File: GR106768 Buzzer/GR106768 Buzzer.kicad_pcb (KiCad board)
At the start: 4 copper layers, 76 x 58 mm, 342 parts, among them IC1 L-BC-SOT23-5, IC2 L-BC-SO08, IC3 L-BC-SO08, IC4 L-BC-SOT23-5, IC5 L-BC-SO08, IC6 L-BC-SO08, IC7 L-BC-SOT23-6, IC8 L-BC-DFN10, IC9 L-BC-SOT23-6, J1 BAR-10-1007, J2 MIRECMS, J3 MIRECMS, SW1 SI-10-NK236, T1 Q-BC-SOT23-BEC, T10 Q-BC-SOT23-GSD, T11 Q-BC-SOT23-GSD, T12 Q-BC-SOT23-GSD, T13 Q-BC-SOT23-GSD, T2 Q-BC-SOT23-BEC, T3 Q-BC-SOT23-BEC, T4 Q-BC-SOT23-BEC, T5 Q-BC-SOT23-GSD, T6 Q-BC-SOT23-GSD, T7 Q-BC-SOT23-GSD, T8 Q-BC-SOT23-GSD, T9 Q-BC-SOT23-GSD

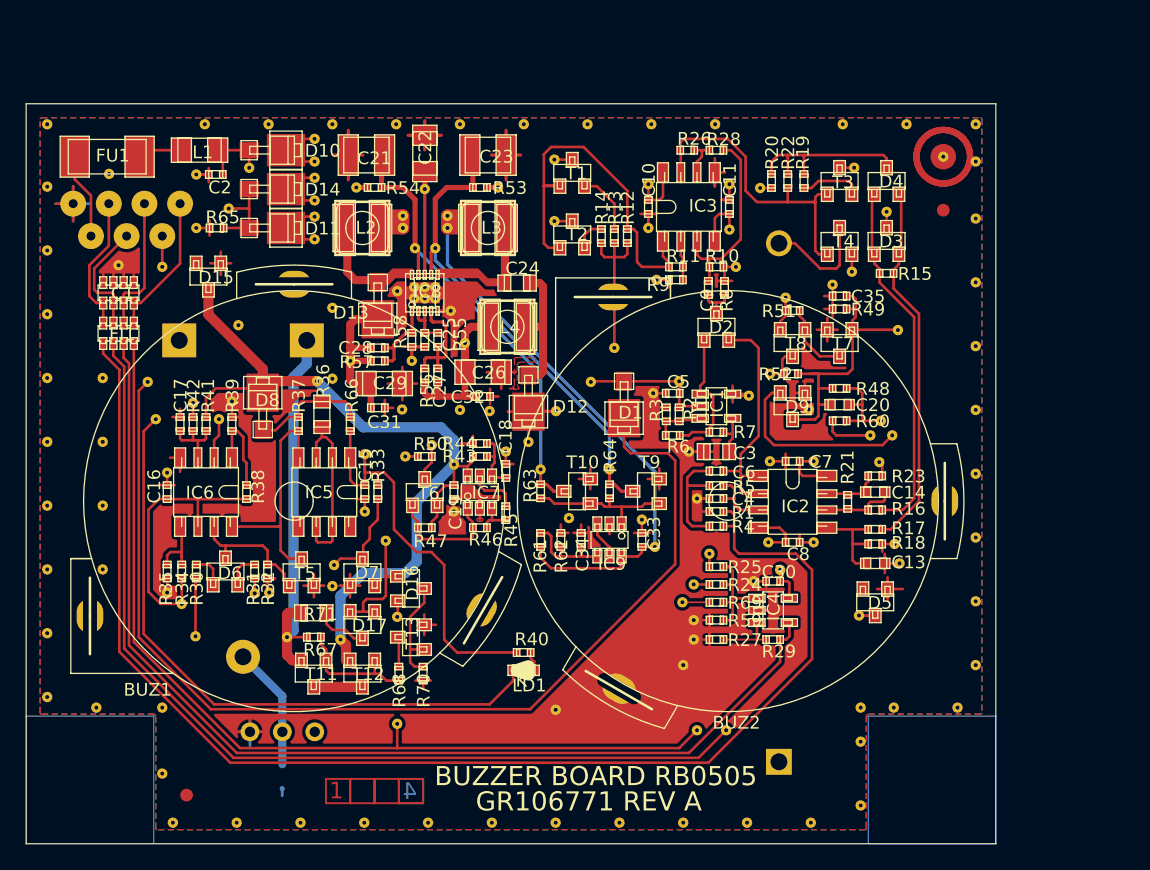
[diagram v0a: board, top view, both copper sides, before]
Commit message: buzzer PCB updates
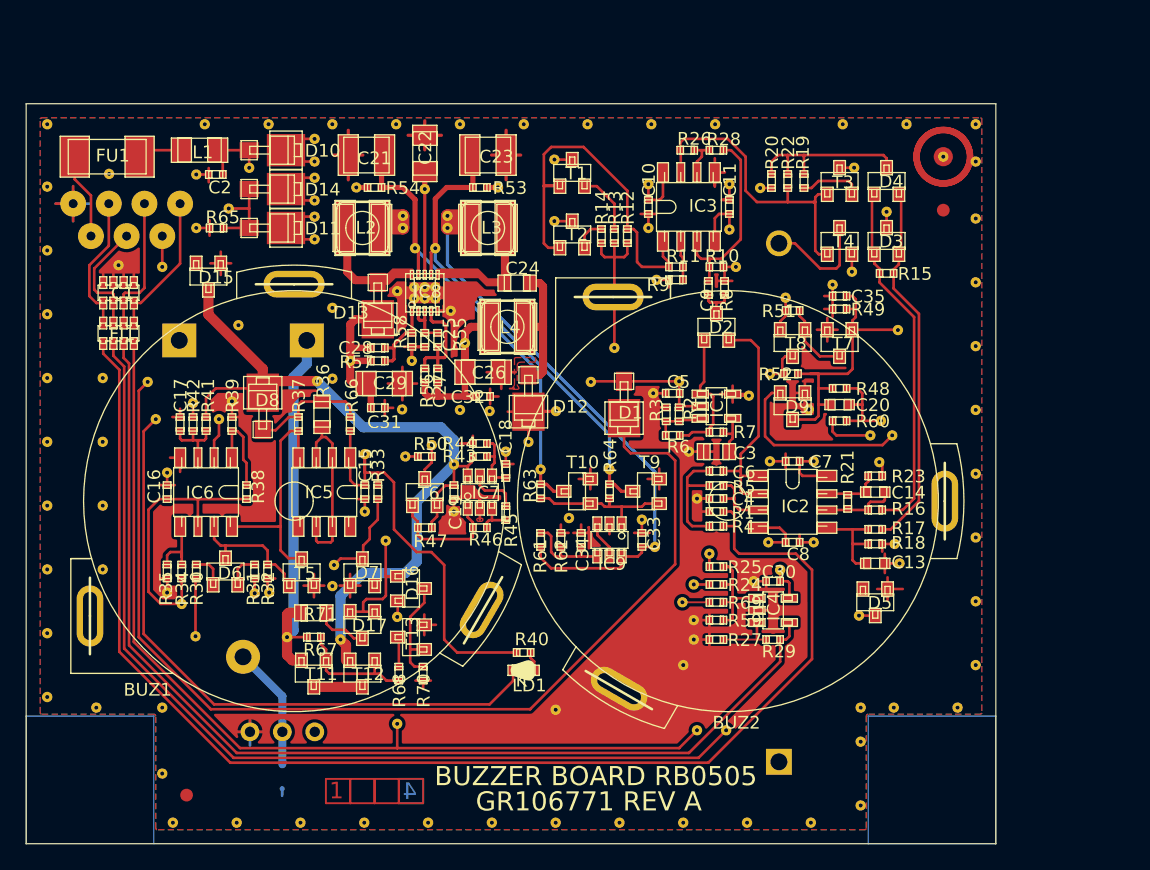
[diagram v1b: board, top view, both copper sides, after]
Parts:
- BUZ1: footprint PKM33EPH-1201C_101110111001 -> AllModules:PKM33EPH-1201C_101110111001
- BUZ2: footprint PKM33EPH-1201C_100110111001 -> AllModules:PKM33EPH-1201C_100110111001
- JP1: footprint TB-CMS-AIROX -> AllModules:TB-CMS-AIROX_1
- V1, V10, V101, V103, V107, V11, V111, V113, V116, V117, V12, V124, V125, V126, V127, V128, V129, V13, V130, V131, V132, V133, V134, V135, V136, V137, V138, V14, V140, V143, V144, V147, V148, V157, V158, V162, V163, V169, V17, V170, V18, V19, V2, V20, V21, V22, V23, V24, V25, V26, V28, V29, V3, V32, V33, V34, V36, V39, V4, V40, V41, V42, V43, V44, V45, V46, V47, V48, V5, V50, V55, V56, V57, V59, V6, V65, V66, V67, V68, V69, V7, V70, V71, V72, V73, V74, V75, V8, V81, V82, V84, V85, V86, V87, V88, V89, V9, V91, V92, V93, V94, V95, V96, V97, V99: value VIA-08X03-VE -> Val**; footprint VIA-08X03-VE -> AllModules:Via_12x32
- V100, V102, V104, V105, V106, V108, V109, V110, V112, V114, V115, V118, V119, V120, V121, V122, V123, V139, V141, V142, V145, V146, V149, V15, V150, V151, V152, V153, V154, V16, V164, V27, V30, V31, V35, V37, V38, V51, V52, V53, V54, V58, V60, V61, V62, V63, V64, V76, V77, V78, V79, V80, V83, V90, V98: value VIA-08X03-VE_1011 -> Val**; footprint VIA-08X03-VE_1011 -> AllModules:Via_12x32-1._.3.4

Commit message: buzzer PCB TH parts and vias
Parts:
- V155, V156, V159, V160, V161, V49: value VIA-08X03-VE_1001 -> Val**; footprint VIA-08X03-VE_1001 -> AllModules:Via_12x32-1._._.4
- V165, V166, V167, V168, V171: value VIA-08X03_1011 -> Val**; footprint VIA-08X03_1011 -> AllModules:Via_12x32-1._.3.4
- V172, V173: value VIA-08X03_1001 -> Val**; footprint VIA-08X03_1001 -> AllModules:Via_12x32-1._._.4

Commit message: buzzer schematic changes
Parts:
- renumbered L2-2 to ZL2, L3-2 to ZL3, L4-2 to ZL4
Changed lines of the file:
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@@
-(kicad_pcb (version 20171130) (host pcbnew 5.1.5-52549c5~86~ubuntu18.04.1)
+(kicad_pcb (version 20171130) (host pcbnew "(5.1.5)-3")
   (general
     (thickness 1.6)
@@
     (solder_mask_min_width 0.25)
     (aux_axis_origin 0 0)
-    (visible_elements FFF7B7A7)
+    (visible_elements 7FFFFFFF)
     (pcbplotparams
       (layerselection 0x010fc_ffffffff)
@@
   (module NR4012 placed (layer F.Cu)
     (at 147.719 79.487 180)
-    (fp_text reference L4-2 (at 0 0 180) (layer F.SilkS) hide
+    (fp_text reference ZL4 (at 0 0 180) (layer F.SilkS) hide
       (effects (font (size 1 1) (thickness 0.15)))
     )
@@
   (module NR4012 placed (layer F.Cu)
     (at 146.195 71.74)
-    (fp_text reference L3-2 (at 0 0) (layer F.SilkS) hide
+    (fp_text reference ZL3 (at 0 0) (layer F.SilkS) hide
       (effects (font (size 1 1) (thickness 0.15)))
     )
@@
   (module NR4018 placed (layer F.Cu)
     (at 136.3525 71.74 180)
-    (fp_text reference L2-2 (at 0 0 180) (layer F.SilkS) hide
+    (fp_text reference ZL2 (at 0 0 180) (layer F.SilkS) hide
       (effects (font (size 1 1) (thickness 0.15)))
     )

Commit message: PCB and schematic updates
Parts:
- BUZ1: footprint AllModules:PKM33EPH-1201C_101110111001 -> PKM33EPH-1201C_101110111001
- BUZ2: footprint AllModules:PKM33EPH-1201C_100110111001 -> PKM33EPH-1201C_100110111001
- JP1: footprint AllModules:TB-CMS-AIROX_1 -> TB-CMS-AIROX
- V172, V173: footprint AllModules:Via_12x32-1._._.4 -> AllModules:Via_12x36-1._._.4
- cam6, cam7, cam8, cam9: footprint COIN_EXTERNE -> AllModules:COIN_EXTERNE_1
- moved C2 11.2 mm to (134.9, 62.5)
- moved V117 11.2 mm to (133.3, 62.5)
- moved D6 11.2 mm to (135.6, 93.7)
- moved IC6 11.2 mm to (134.1, 87.4)
- moved J3 11.2 mm to (132.6, 111.2)
- moved R30 11.2 mm to (133.3, 93.7)
- moved R31 11.2 mm to (137.9, 93.7)
- moved R34 11.2 mm to (132.2, 93.7)
- moved R41 11.2 mm to (134.1, 82.1)
- moved R65 11.2 mm to (134.9, 66.7)
- moved V139 11.2 mm to (132.2, 96.2)
- moved V148 11.2 mm to (133.3, 66.7)
- moved V30 11.2 mm to (137.9, 95.4)
- moved C21 11.2 mm to (146.7, 61.0)
- moved C23 11.2 mm to (156.2, 61.0)
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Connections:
- net /+12V renamed +12V
- net /+5V renamed +5V
- net /-12V renamed -12V
- BAT1 pad +: /BATTV -> BATTV
- R67 pad 2: /BATTV -> BATTV
- R71 pad 2: /BATTV -> BATTV
- T11 pad S: /BATTV -> BATTV
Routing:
- net BATTV: track 0.00 -> 31.1 mm
- net /BATTV: track 31.1 -> 0.00 mm
- net GND: track 465.3 -> 466.4 mm
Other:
- rule trace_min: 0.1 -> 0.2
- board text added: "7 white wire UL 1061 AWG26"
- board text added: "C12 et BAT1 doivent etre colles. Voir plan 40966.E04.000. C12 and BAT1 must be glued Refer to drawing 40966.E04.000."
- board text removed: "7 white wires UL 1061 AWG26"
- board text removed: "C12 et BAT1 doivent etre colles. Voir plan 40966.E04.000. C12 and BAT1 must be glued. Refer to drawing 40966.E04.000."
- board text removed: "cam14"

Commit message: Update holes 3
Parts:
- BAT1: value BAT-BT-4-V150H-4.8V -> BT-4-V150H-4.8V_1; footprint BT-4-V150H-4.8V_100110011001 -> AllModules:BT-4-V150H-4.8V_100110011001
- BUZ1: value BZ-10-PKM33EPH-1201C -> PKM33EPH; footprint PKM33EPH-1201C_101110111001 -> AllModules:PKM33EPH-1201C_101110111001
- BUZ2: value BZ-10-PKM33EPH-1201C -> PKM33EPH; footprint PKM33EPH-1201C_100110111001 -> AllModules:PKM33EPH-1201C_100110111001
- C1: value CC-BC-C0612 -> 47pF; footprint C0612-4 -> AllModules:C0612-4_1
- C10, C11, C15, C16, C17, C18, C19, C25, C30, C31, C32, C33, C5, C7, C8, C9: value C-BC-C0402 -> 100nF; footprint C0402 -> AllModules:C0402_1b
- C12: value C-BTP-AX10X30 -> 470μF; footprint AX10X30_10111011 -> AllModules:AX10X30_10111011
- C13, C14: value C-BC-C0603 -> 33nF; footprint C0603 -> AllModules:C0603_1b
- C2: value C-BC-C0402 -> 220pF; footprint C0402 -> AllModules:C0402_1b
- C20: value C-BC-C0603 -> 330nF; footprint C0603 -> AllModules:C0603_1b
- C21, C23: value C-BC-C1210 -> 47μF; footprint C1210 -> AllModules:C1210_1
- C22, C26, C29: value C-BC-C1206 -> 10μF; footprint RC1206 -> AllModules:RC1206_1
- C24: value C-BC-C0805 -> 1uF; footprint C0805 -> AllModules:C0805_1b
- C27, C28: value C-BC-C0402 -> 100pF; footprint C0402 -> AllModules:C0402_1b
- C3: value C-BC-C0805 -> 10nF; footprint C0805 -> AllModules:C0805_1b
- C34: value C-BC-C0402 -> DNP; footprint C0402 -> AllModules:C0402_1b
- C35: value C-BC-C0402 -> 4.7nF; footprint C0402 -> AllModules:C0402_1b
- C4, C6: value C-BC-C0402 -> 680pF; footprint C0402 -> AllModules:C0402_1b
- D1: value D-BC-POWERMITE -> DNP; footprint DO216AA -> AllModules:DO216AA_1
- D10, D11, D12, D13, D14, D8: value D-BC-POWERMITE -> MBRM120; footprint DO216AA -> AllModules:DO216AA_1
- D15: value D-BC-SOT23 -> BZX84B6V8; footprint SOT23-1G -> AllModules:SOT23-1G_1
- D16, D17, D2, D6: value D-BC-SOT23 -> BAT54C; footprint SOT23-1G -> AllModules:SOT23-1G_1
- D3, D4, D9: value D-BC-SOT23 -> BAT54S; footprint SOT23-1G -> AllModules:SOT23-1G_1
- D5: value D-BC-SOT23 -> BZX84C2V7; footprint SOT23-1G -> AllModules:SOT23-1G_1
- D7: value D-BC-SOT23 -> BZX84C5V1; footprint SOT23-1G -> AllModules:SOT23-1G_1
- FI1: value SF-BC-WEFA -> BK32164M102-T; footprint WE-FA -> AllModules:WE-FA_1
- FU1: value FU-BC-R451 -> 500mA; footprint F6126 -> AllModules:F6126_1
- IC1: value L-BC-SOT23-5 -> LMC7211; footprint SOT23-5 -> AllModules:SOT23-5_1
- IC2, IC3: value L-BC-SO08 -> MC33172; footprint MX.A8_COMPOSANT -> AllModules:MX.A8_COMPOSANT_1
- IC4: value L-BC-SOT23-5 -> LMV321; footprint SOT23-5 -> AllModules:SOT23-5_1
- IC5: value L-BC-SO08 -> LM317L_SO8; footprint MX.A8_COMPOSANT -> AllModules:MX.A8_COMPOSANT_1
- IC6: value L-BC-SO08 -> BQ2002C; footprint MX.A8_COMPOSANT -> AllModules:MX.A8_COMPOSANT_1
- IC7, IC9: value L-BC-SOT23-6 -> TLV3011; footprint SOT23-6 -> AllModules:SOT23-6_1
- IC8: value L-BC-DFN10 -> LT3471; footprint DFN10 -> AllModules:DFN10_1
- J1: value BAR-10-1007 -> to CPU board; footprint BAR7-3-2-COVIDIEN_1111100110011001100110011001 -> AllModules:BAR7-3-2-COVIDIEN_1111100110011001100110011001
- J2, J3: footprint MIRECMS-SAFT -> AllModules:MIRECMS-SAFT_1
- JP1: value TB-CMS-AIROX -> DNP; footprint TB-CMS-AIROX -> AllModules:TB-CMS-AIROX_1
- L1: value SF-BC-S1206 -> Core_Ferrite; footprint RC1206 -> AllModules:RC1206_1
- L2: value SF-BC-WETPCS -> 10μH; footprint WETPC-S -> AllModules:WETPC-S_1
- L3, L4: value SF-BC-WETPCS -> 15μH; footprint WETPC-S -> AllModules:WETPC-S_1
- LD1: value LED-BC-D0603 -> DNP; footprint D0603 -> AllModules:D0603_1
- R1, R10, R2, R24, R29, R3, R38, R39, R42, R47, R59, R63, R64, R67: value R-BC-R0402 -> 100k; footprint R0402 -> AllModules:R0402_1
- R11: value R-BC-R0402 -> 105k; footprint R0402 -> AllModules:R0402_1
- R12, R22: value R-BC-R0402 -> 470; footprint R0402 -> AllModules:R0402_1
- R13, R14, R19, R20: value R-BC-R0402 -> 1.5; footprint R0402 -> AllModules:R0402_1
- R15: value R-BC-R0402 -> 33; footprint R0402 -> AllModules:R0402_1
- R16, R17, R32, R34, R4, R49, R5, R51, R52, R61, R62, R66, R68, R70: value R-BC-R0402 -> 10k; footprint R0402 -> AllModules:R0402_1
- R18, R21: value R-BC-R0402 -> 150k; footprint R0402 -> AllModules:R0402_1
- R23, R65: value R-BC-R0402 -> 2.2k; footprint R0402 -> AllModules:R0402_1
- R25, R48, R50, R60: value R-BC-R0402 -> DNP; footprint R0402 -> AllModules:R0402_1
- R26: value R-BC-R0402 -> 137k; footprint R0402 -> AllModules:R0402_1
- R27: value R-BC-R0402 -> 68k; footprint R0402 -> AllModules:R0402_1
- R28, R9: value R-BC-R0402 -> 32.4k; footprint R0402 -> AllModules:R0402_1
- R30, R31: value R-BC-R0402 -> 0; footprint R0402 -> AllModules:R0402_1
- R33, R8: value R-BC-R0402 -> 1k; footprint R0402 -> AllModules:R0402_1
- R35: value R-BC-R0402 -> 33k; footprint R0402 -> AllModules:R0402_1
- R36: value R-BC-R0805 -> 33; footprint R0805 -> AllModules:R0805_1b
- R37: value R-BC-R0402 -> 220; footprint R0402 -> AllModules:R0402_1
- R40: value R-BC-R0402 -> 4.7k; footprint R0402 -> AllModules:R0402_1
- R41: value R-BC-R0402 -> 180k; footprint R0402 -> AllModules:R0402_1
- R43: value R-BC-R0402 -> 1.5M; footprint R0402 -> AllModules:R0402_1
- R44: value R-BC-R0402 -> 680k; footprint R0402 -> AllModules:R0402_1
- R45, R6: value R-BC-R0402 -> 59k; footprint R0402 -> AllModules:R0402_1
- R46: value R-BC-R0402 -> 1M; footprint R0402 -> AllModules:R0402_1
- R53, R54: value R-BC-R0402 -> 47k; footprint R0402 -> AllModules:R0402_1
- R55: value R-BC-R0402 -> 15k; footprint R0402 -> AllModules:R0402_1
- R56: value R-BC-R0402 -> 182k; footprint R0402 -> AllModules:R0402_1
- R57: value R-BC-R0402 -> 54.9k; footprint R0402 -> AllModules:R0402_1
- R58: value R-BC-R0402 -> 4.99k; footprint R0402 -> AllModules:R0402_1
- R69: value R-BC-R0402 -> 200k; footprint R0402 -> AllModules:R0402_1
- R7: value R-BC-R0402 -> 51.1k; footprint R0402 -> AllModules:R0402_1
- R71: value R-BC-R0805 -> 470; footprint R0805 -> AllModules:R0805_1b
- SJ1: value TB-CMS-AIROX -> Jumper_Small; footprint TB-CMS-AIROX-2 -> AllModules:TB-CMS-AIROX-2_1
- SW1: value SI-10-NK236 -> NK236_; footprint NK236_1_100110011111 -> AllModules:NK236_100110011111
- T1, T3: value Q-BC-SOT23-BEC -> BC847; footprint SOT23-BEC -> AllModules:SOT23-BEC_1
- T10, T13, T5, T7, T9: value Q-BC-SOT23-GSD -> Si2312BDS; footprint SOT23-GSD -> AllModules:SOT23-GSD_1
- T11, T12, T6, T8: value Q-BC-SOT23-GSD -> Si2315BDS; footprint SOT23-GSD -> AllModules:SOT23-GSD_1
- T2, T4: value Q-BC-SOT23-BEC -> BC857; footprint SOT23-BEC -> AllModules:SOT23-BEC_1
- V1, V10, V101, V103, V107, V11, V111, V113, V116, V117, V12, V124, V125, V126, V127, V128, V129, V13, V130, V131, V132, V133, V134, V135, V136, V137, V138, V14, V140, V143, V144, V147, V148, V157, V158, V162, V163, V169, V17, V170, V18, V19, V2, V20, V21, V22, V23, V24, V25, V26, V28, V29, V3, V32, V33, V34, V36, V39, V4, V40, V41, V42, V43, V44, V45, V46, V47, V48, V5, V50, V55, V56, V57, V59, V6, V65, V66, V67, V68, V69, V7, V70, V71, V72, V73, V74, V75, V8, V81, V82, V84, V85, V86, V87, V88, V89, V9, V91, V92, V93, V94, V95, V96, V97, V99: value Val** -> GND
- V100, V114: value Val** -> N$18; footprint AllModules:Via_12x32-1._.3.4 -> AllModules:Via_12x32
- V102, V105, V110, V115, V120, V123, V149, V150, V151, V152, V153, V154: value Val** -> N$10; footprint AllModules:Via_12x32-1._.3.4 -> AllModules:Via_12x32
- V104, V106, V38, V83: value Val** -> -12V; footprint AllModules:Via_12x32-1._.3.4 -> AllModules:Via_12x32
- V108, V30, V77, V78, V79: value Val** -> SUPPLY-BUZ; footprint AllModules:Via_12x32-1._.3.4 -> AllModules:Via_12x32
- V109: value Val** -> N$31; footprint AllModules:Via_12x32-1._.3.4 -> AllModules:Via_12x32
- V112, V119, V121, V51, V53, V80: value Val** -> +12V; footprint AllModules:Via_12x32-1._.3.4 -> AllModules:Via_12x32
- V118, V167, V35, V54, V60: value Val** -> +5V; footprint AllModules:Via_12x32-1._.3.4 -> AllModules:Via_12x32
- V122, V142: value Val** -> GT1; footprint AllModules:Via_12x32-1._.3.4 -> AllModules:Via_12x32
- V139, V164: value Val** -> N$58; footprint AllModules:Via_12x32-1._.3.4 -> AllModules:Via_12x32
- V141: value Val** -> N$19; footprint AllModules:Via_12x32-1._.3.4 -> AllModules:Via_12x32
- V145, V166, V168: value Val** -> GND; footprint AllModules:Via_12x32-1._.3.4 -> AllModules:Via_12x32
- V146, V27, V31, V52: value Val** -> BUZ-ACT; footprint AllModules:Via_12x32-1._.3.4 -> AllModules:Via_12x32
- V15, V61: value Val** -> INHIB-STOP-INV; footprint AllModules:Via_12x32-1._.3.4 -> AllModules:Via_12x32
- V155, V161: value Val** -> SHDN1; footprint AllModules:Via_12x32-1._._.4 -> AllModules:Via_12x32
- V156, V160: value Val** -> SHDN2; footprint AllModules:Via_12x32-1._._.4 -> AllModules:Via_12x32
- V159: value Val** -> GND; footprint AllModules:Via_12x32-1._._.4 -> AllModules:Via_12x32
- V16, V64: value Val** -> STOP-INV; footprint AllModules:Via_12x32-1._.3.4 -> AllModules:Via_12x32
- V165, V171: value Val** -> VCHARG; footprint AllModules:Via_12x32-1._.3.4 -> AllModules:Via_12x32
- V172: value Val** -> +BATTV; footprint AllModules:Via_12x36-1._._.4 -> AllModules:Via_12x32
- V173: value Val** -> VCHARG; footprint AllModules:Via_12x36-1._._.4 -> AllModules:Via_12x32
- V37, V58, V90: value Val** -> VBAT; footprint AllModules:Via_12x32-1._.3.4 -> AllModules:Via_12x32
- V49: value Val** -> VCHARG; footprint AllModules:Via_12x32-1._._.4 -> AllModules:Via_12x32
- V62, V63: value Val** -> N$78; footprint AllModules:Via_12x32-1._.3.4 -> AllModules:Via_12x32
- V76, V98: value Val** -> SUPPLY-BUZ-CPU; footprint AllModules:Via_12x32-1._.3.4 -> AllModules:Via_12x32
- ZL2: value SF-BC-NR4018 -> DNP; footprint NR4018 -> AllModules:NR4018_1
- ZL3, ZL4: value SF-BC-NR4012 -> DNP; footprint NR4012 -> AllModules:NR4012_1
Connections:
- net /BUZ-ACT renamed BUZ-ACT
- net /GT1 renamed GT1
- net /INHIB-STOP-INV renamed INHIB-STOP-INV
- net /N$1 renamed /GR106768_buzzer_charger/N$1
- net /N$10 renamed N$10
- net /N$18 renamed N$18
- net /N$19 renamed N$19
- net /N$22 renamed /GR106768_buzzer_charger/N$22
- net /N$23 renamed /GR106768_buzzer_charger/N$23
- net /N$29 renamed /GR106768_buzzer_charger/N$29
- net /N$31 renamed N$31
- net /N$33 renamed /GR106768_buzzer_charger/N$33
- net /N$34 renamed /GR106768_buzzer_charger/N$34
- net /N$36 renamed /GR106768_buzzer_charger/N$36
- net /N$38 renamed /GR106768_buzzer_charger/N$38
- net /N$40 renamed /GR106768_buzzer_charger/N$40
- net /N$41 renamed /GR106768_buzzer_charger/N$41
- net /N$42 renamed /GR106768_buzzer_charger/N$42
- net /N$43 renamed /GR106768_buzzer_charger/N$43
- net /N$44 renamed /GR106768_buzzer_charger/N$44
- net /N$46 renamed /GR106768_buzzer_charger/N$46
- net /N$47 renamed /GR106768_buzzer_charger/N$47
- net /N$48 renamed /GR106768_buzzer_charger/N$48
- net /N$49 renamed /GR106768_buzzer_charger/N$49
- net /N$50 renamed /GR106768_buzzer_charger/N$50
- net /N$51 renamed /GR106768_buzzer_charger/N$51
- net /N$52 renamed /GR106768_buzzer_charger/N$52
- net /N$53 renamed /GR106768_buzzer_charger/N$53
- net /N$54 renamed /GR106768_buzzer_charger/N$54
- net /N$55 renamed /GR106768_buzzer_charger/N$55
- net /N$56 renamed /GR106768_buzzer_charger/N$56
- net /N$57 renamed /GR106768_buzzer_charger/N$57
- net /N$58 renamed N$58
- net /N$59 renamed /GR106768_buzzer_charger/N$59
- net /N$6 renamed /GR106768_buzzer_charger/N$6
- net /N$78 renamed N$78
- net /N$8 renamed /GR106768_buzzer_charger/N$8
- net /N$9 renamed /GR106768_buzzer_charger/N$9
- net /SHDN1 renamed SHDN1
- net /SHDN2 renamed SHDN2
- net /STOP-INV renamed STOP-INV
- net /SUPPLY-BUZ renamed SUPPLY-BUZ
- net /SUPPLY-BUZ-CPU renamed SUPPLY-BUZ-CPU
- net /VBAT renamed VBAT
- BAT1 pad +: BATTV -> +BATTV
- BAT1 pad -: /N$20 -> /GR106768_buzzer_charger/N$20
- BAT1 pad 3: (no net) -> Net-(BAT1-Pad3)
- BUZ1 pad 3: (no net) -> Net-(BUZ1-Pad3)
- BUZ2 pad 3: (no net) -> Net-(BUZ2-Pad3)
- C19 pad 1: /VCHARG -> VCHARG
- D15 pad 2: (no net) -> Net-(D15-Pad2)
- D15 pad 3: /VCHARG -> VCHARG
- D5 pad 2: (no net) -> Net-(D5-Pad2)
- D7 pad 2: (no net) -> Net-(D7-Pad2)
- D8 pad K: /VCHARG -> VCHARG
- IC5 pad 5: (no net) -> Net-(IC5-Pad5)
- IC5 pad 8: (no net) -> Net-(IC5-Pad8)
- IC7 pad 6: /VCHARG -> VCHARG
- R41 pad 1: /VCHARG -> VCHARG
- R43 pad 2: /VCHARG -> VCHARG
- R47 pad 2: /VCHARG -> VCHARG
- R67 pad 2: BATTV -> +BATTV
- R69 pad 1: /VCHARG -> VCHARG
- R71 pad 2: BATTV -> +BATTV
- SJ1 pad 1: GND -> /GR106768_buzzer_charger/N$20
- SJ1 pad 2: /N$20 -> GND
- SW1 pad 1: /N$20 -> /GR106768_buzzer_charger/N$20
- SW1 pad 2: (no net) -> Net-(SW1-Pad2)
- T11 pad S: BATTV -> +BATTV
- T12 pad S: /VCHARG -> VCHARG
- T6 pad S: /VCHARG -> VCHARG
- V165 pad ~: /VCHARG -> VCHARG
- V171 pad ~: /VCHARG -> VCHARG
- V49 pad ~: /VCHARG -> VCHARG
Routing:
- net VCHARG: track 0.00 -> 98.1 mm
- net /VCHARG: track 98.1 -> 0.00 mm
- net BATTV: track 31.1 -> 0.00 mm
- net +BATTV: track 0.00 -> 31.1 mm
- net /N$20: track 9.70 -> 0.00 mm
- net /GR106768_buzzer_charger/N$20: track 0.00 -> 9.70 mm
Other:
- rule trace_min: 0.2 -> 0.05

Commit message: Update holes 4
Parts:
- SJ1: footprint AllModules:TB-CMS-AIROX-2_1 -> AllModules:TB-CMS-AIROX-2
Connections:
- SJ1 pad 1: /GR106768_buzzer_charger/N$20 -> GND
- SJ1 pad 2: GND -> /GR106768_buzzer_charger/N$20
